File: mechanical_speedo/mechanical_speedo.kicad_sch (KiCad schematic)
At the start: 27 parts, among them J1 Conn_01x08, J2 Conn_01x04, J3 Conn_01x03, J4 Conn_01x03, SW1 JS5208, U1 Teensy4.0, U2 TJA1050T/CM,118, U3 L6234PD, U6 LD1117S18TR_SOT223

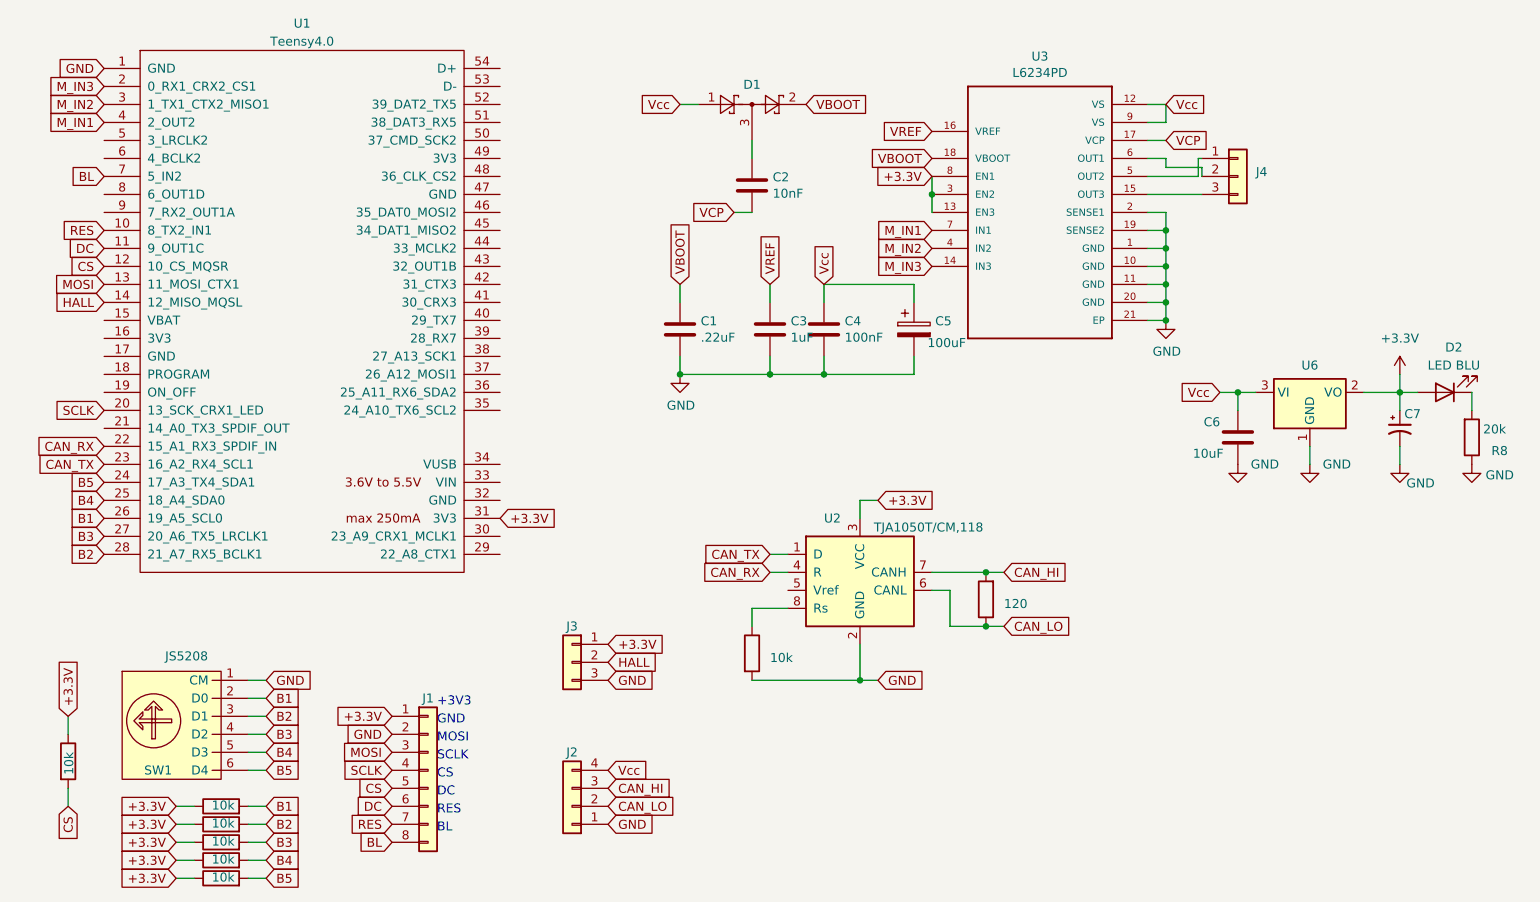
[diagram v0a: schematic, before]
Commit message: added encoder board to mechanical_speedo
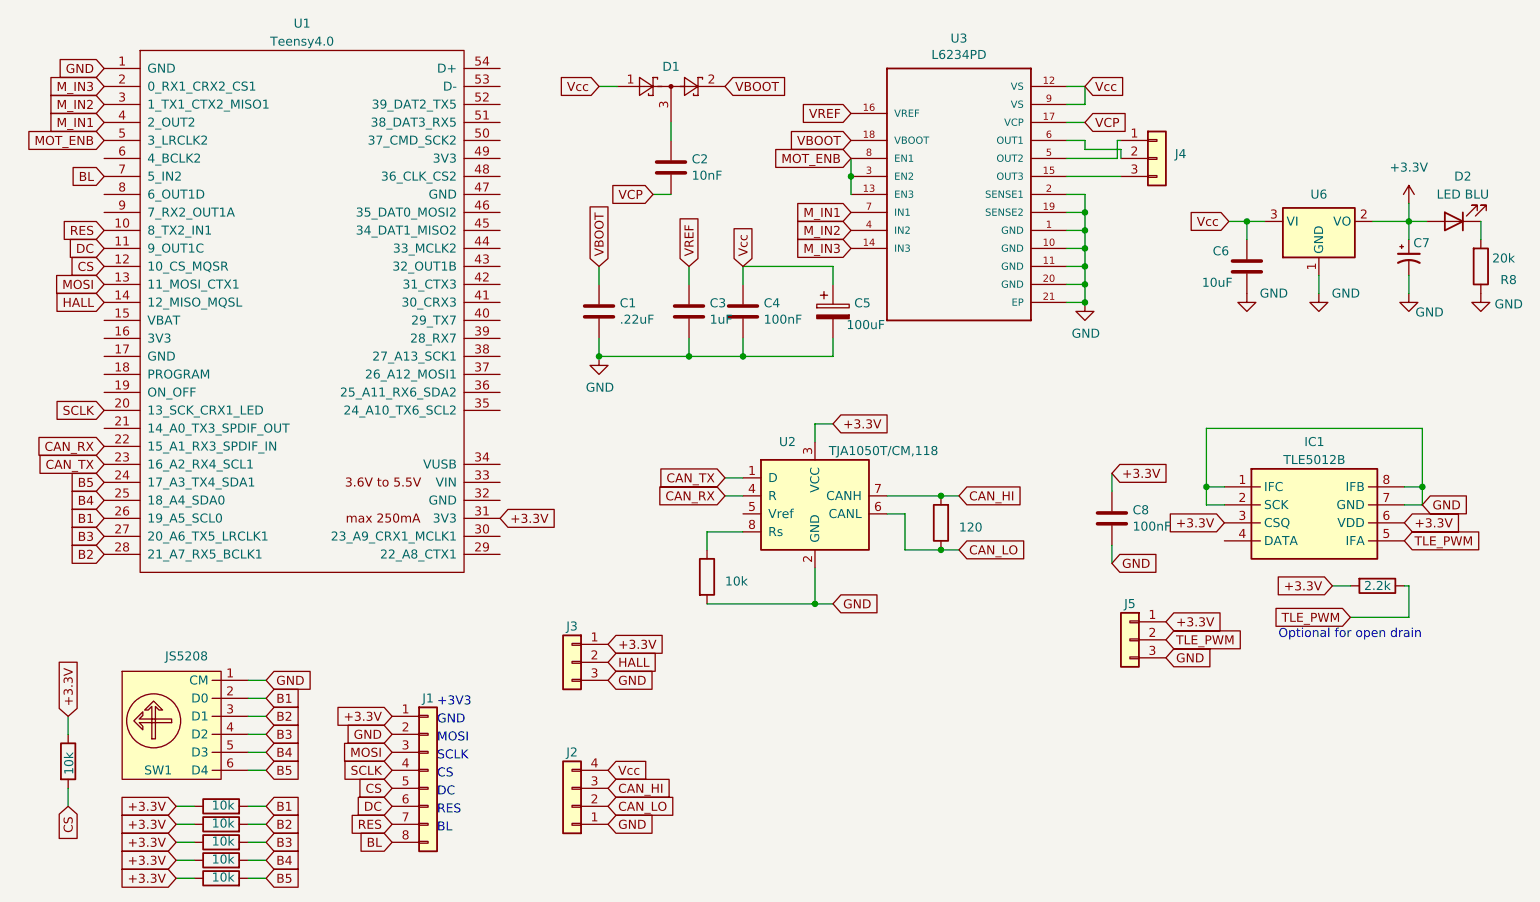
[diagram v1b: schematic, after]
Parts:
- added C8: 100nF, Capacitor_SMD:C_0603_1608Metric, symbol Device:C
- added IC1: TLE5012B, TLE5012:SOIC127P600X175-8N, symbol TLE5012BE5000XUMA1:TLE5012BE5000XUMA1
- added J5: Conn_01x03, Connector_PinHeader_2.54mm:PinHeader_1x03_P2.54mm_Vertical, symbol Connector_Generic:Conn_01x03
- added R11: 2.2k, Resistor_SMD:R_0603_1608Metric, symbol Device:R
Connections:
- net +3.3V: now also C8.1, IC1.3 (CSQ), IC1.6 (VDD), J5.1 (Pin_1), R11.2; no longer U3.13 (EN3), U3.3 (EN2), U3.8 (EN1)
- net GND: now also C8.2, IC1.1 (IFC), IC1.2 (SCK), IC1.7 (GND), IC1.8 (IFB), J5.3 (Pin_3)
- net MOT_ENB: now reaches U1.5 (3_LRCLK2)
- net MOT_ENB: now also U3.13 (EN3), U3.3 (EN2), U3.8 (EN1)
- new net TLE_PWM: IC1.5 (IFA), J5.2 (Pin_2), R11.1
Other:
- note added: "Optional for open drain"
- moved on the sheet: C1, C2, C3, C4, C5, C6, C7, D1, D2, J4, R8, U2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
